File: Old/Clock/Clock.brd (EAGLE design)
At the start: 36.3 x 29.8 mm, 18 parts, among them T1 therm

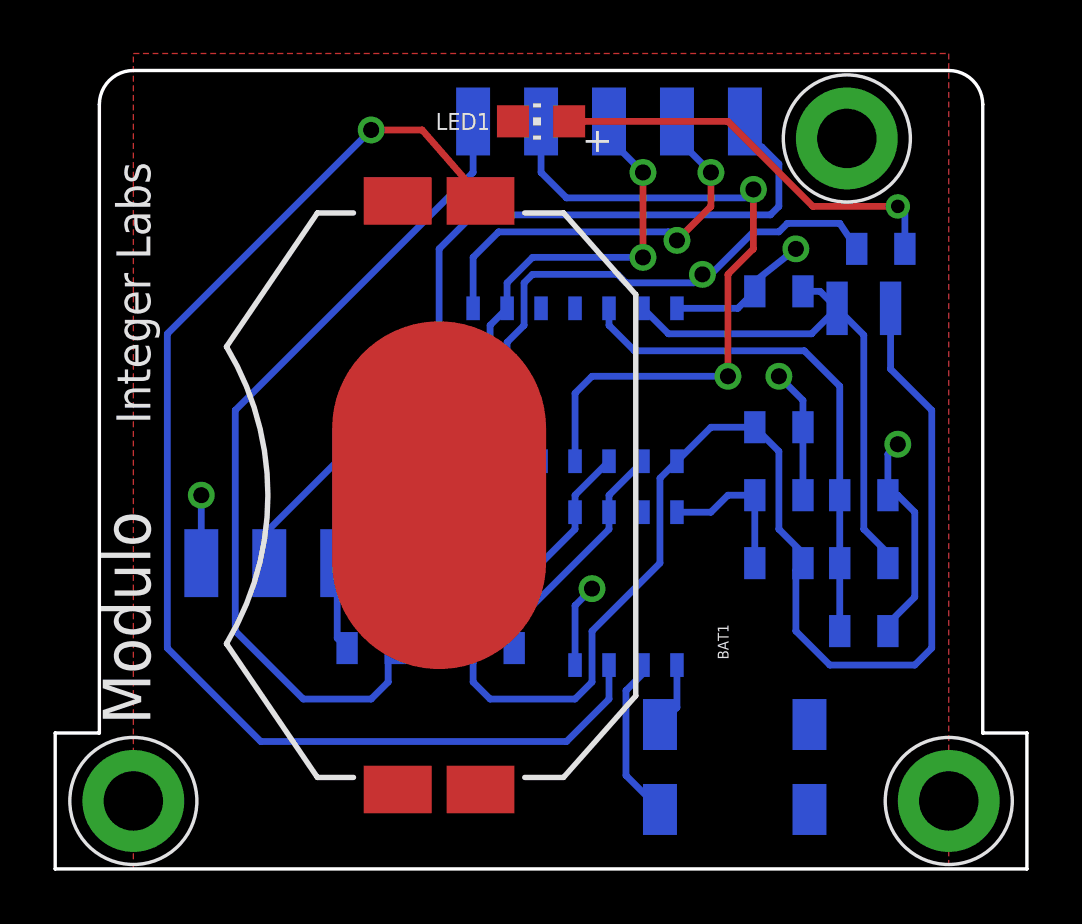
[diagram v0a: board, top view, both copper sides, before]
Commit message: Moved a bunch of files around
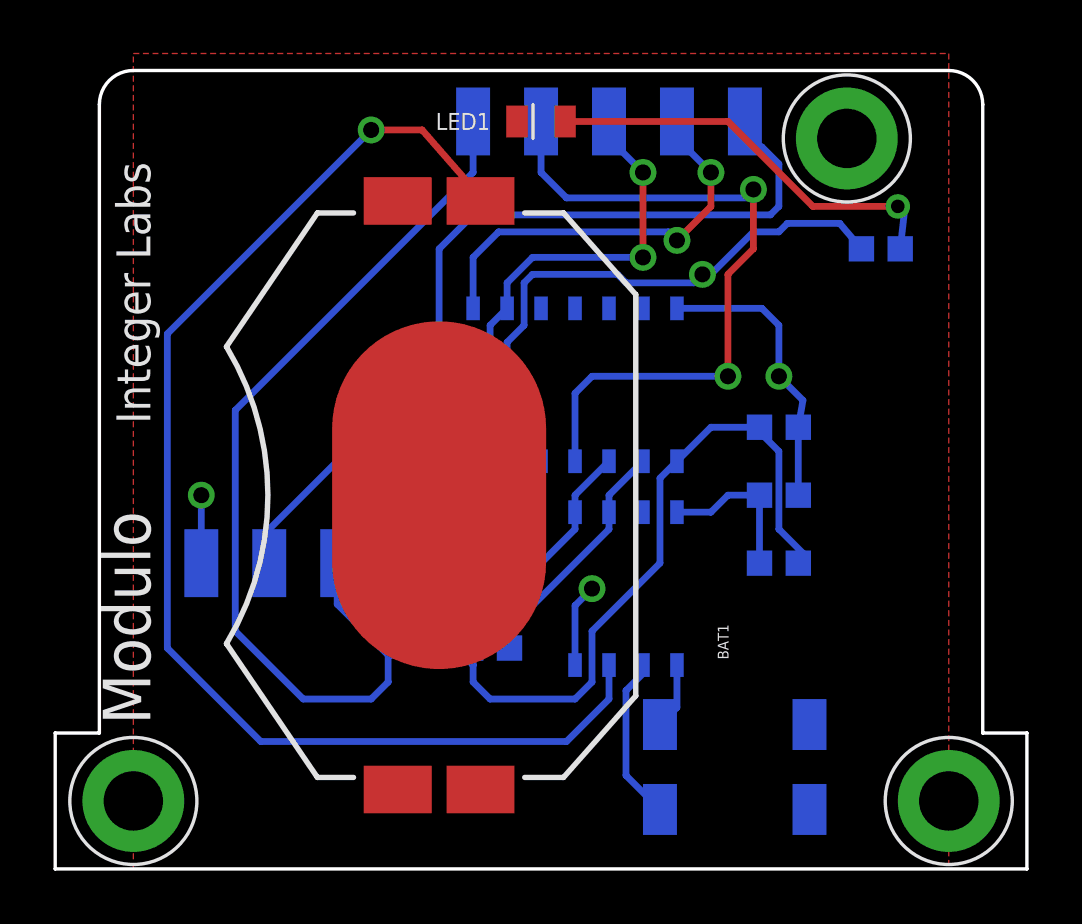
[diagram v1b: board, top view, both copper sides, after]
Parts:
- removed C3: .1uF, SparkFun-Capacitors:0805
- removed C4: .47uF, SparkFun-Capacitors:0805
- removed L1: 1mH, SparkFun-Passives:1007
- removed R2: 10k, SparkFun-Passives:0805
- removed R4: 1, SparkFun-Resistors:0805
- removed T1: therm, SparkFun-Passives:0805
- removed U$3: TINY841, IntegerLabs:SOIC14
- removed U$4: FOOTPRINTFOOTPRINT-2, IntegerLabs:FOOTPRINT2
- added U1: ATTINY841, Modulo:SOIC-14
- added U3: EXCLUDE, Modulo:DEVICE-PCB
- C1: value .47uF -> 100nF; device SparkFun-Capacitors:0805 -> Modulo:0603
- C2: device SparkFun-Passives:0805 -> Modulo:0603
- LED1: value (none) -> blue; device adafruit:CHIP-LED0805 -> Modulo:0805-LED
- R1: value 680 -> 681Ω; device SparkFun-Passives:0805 -> Modulo:0603
- R3: value 1k -> 1KΩ; device SparkFun-Passives:0805 -> Modulo:0603
- R5, R6: value 2k -> 1.5KΩ; device SparkFun-Resistors:0805 -> Modulo:0603
- renumbered U$1 to X1, U$2 to U2
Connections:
- removed net AVCC: C4.2, L1.1, R2.1, U$3.13
- removed net N$2: R4.2, U$4.BUS2
- removed net THERM: C3.1, R2.2, T1.2, U$3.12
- net GND: now also U1.14, U3.BUS0; no longer C3.2, C4.1, T1.1, U$3.14, U$4.BUS0
- net LED: now also U1.6; no longer U$3.6
- net MISO: now also U1.8, U3.PROG3; no longer U$3.8, U$4.PROG3
- net RESET: now also U1.4, U3.PROG1; no longer U$3.4, U$4.PROG1
- net RTC_SCL: now also U1.2; no longer U$3.2
- net RTC_SDA: now also U1.3; no longer U$3.3
- net SCL/SCK: now also U1.9, U3.BUS3, U3.PROG2; no longer U$3.9, U$4.BUS3, U$4.PROG2
- net SDA/MOSI: now also U1.7, U3.BUS1, U3.PROG4; no longer U$3.7, U$4.BUS1, U$4.PROG4
- net VCC: now also U1.1, U3.BUS2, U3.PROG0; no longer L1.2, R4.1, U$3.1, U$4.PROG0
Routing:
- net AVCC: track 19.9 -> 0.00 mm
- net THERM: track 19.4 -> 0.00 mm
- net VCC: track 84.0 -> 66.7 mm
- net GND: track 28.0 -> 20.3 mm, vias 5 -> 3
- net N$2: track 3.33 -> 0.00 mm
